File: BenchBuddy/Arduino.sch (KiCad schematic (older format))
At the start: 0 parts

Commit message: Week3 Part 2
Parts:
- added ARD?: ARDUINOPINS, symbol ARDUINOPINS
- added R? (x14): R, ~, symbol R
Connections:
- net labels added: +12P, ADC_CS_N, CURR_MEAS, DAC_CS_N, FAN_MODE, FAN_PWM, GND, LED_EN_PWM, RELAY+, RELAY-, V+_ADJ_MON, V-_ADJ_MON
- net labels removed: CS_N, FAN_EN, LED_EN, LED_FREQ, Relay+, Relay-
- wire segments 0 -> 31

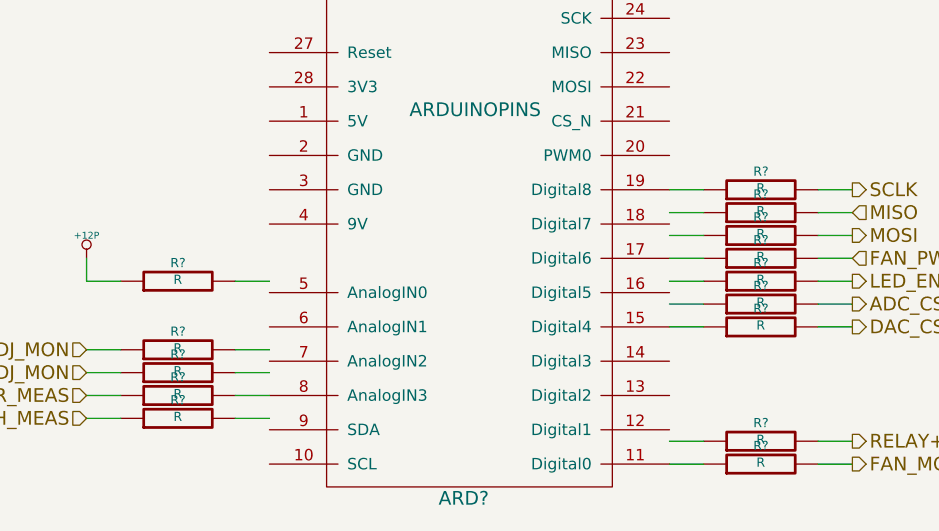
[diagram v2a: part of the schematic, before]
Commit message: Colocação dos Componentes Relé
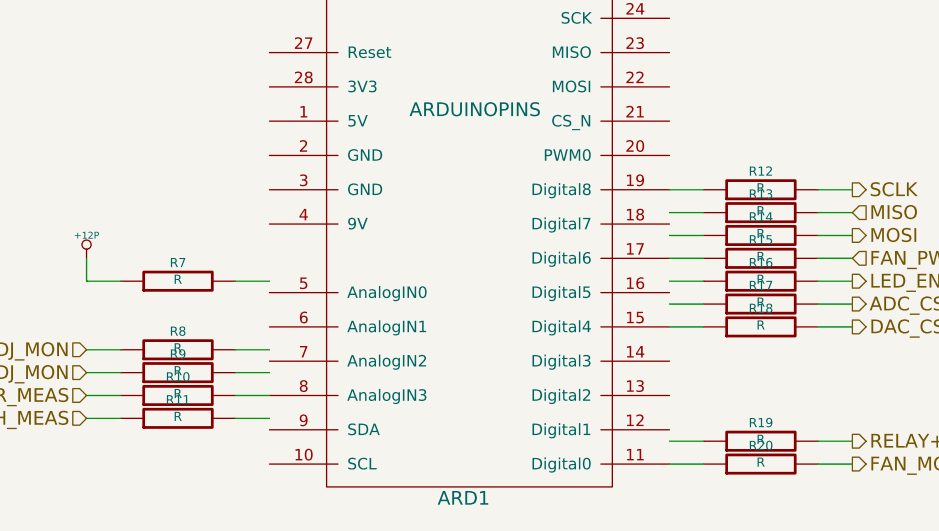
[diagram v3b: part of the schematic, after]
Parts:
- gave numbers to parts that had none: 15
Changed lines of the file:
@@
 Sheet 2 9
 Title ""
-Date "7 mar 2014"
+Date "9 mar 2014"
 Rev ""
 Comp ""
@@
 TACH_MEAS
 $Comp
-L ARDUINOPINS ARD?
+L ARDUINOPINS ARD1
 U 1 1 5319A07F
 P 6200 2900
-F 0 "ARD?" H 6200 2500 60  0000 C CNN
+F 0 "ARD1" H 6200 2500 60  0000 C CNN
 F 1 "ARDUINOPINS" H 6250 4200 60  0000 C CNN
 F 2 "" H 6100 2600 60  0000 C CNN
@@
 CURR_MEAS
 $Comp
-L R R?
+L R R15
 U 1 1 5319A0B5
 P 7500 2250
-F 0 "R?" V 7580 2250 40  0000 C CNN
+F 0 "R15" V 7580 2250 40  0000 C CNN
 F 1 "R" V 7507 2251 40  0000 C CNN
 F 2 "~" V 7430 2250 30  0000 C CNN
@@
 	7750 2250 7900 2250
 $Comp
-L R R?
+L R R19
 U 1 1 5319AB88
 P 7500 3050
-F 0 "R?" V 7580 3050 40  0000 C CNN
+F 0 "R19" V 7580 3050 40  0000 C CNN
 F 1 "R" V 7507 3051 40  0000 C CNN
 F 2 "~" V 7430 3050 30  0000 C CNN
@@
 	9600 2750 9600 3050
 $Comp
-L GND #PWR?
+L GND #PWR2
 U 1 1 5319ABAC
 P 9600 3050
-F 0 "#PWR?" H 9600 3050 30  0001 C CNN
+F 0 "#PWR2" H 9600 3050 30  0001 C CNN
 F 1 "GND" H 9600 2980 30  0001 C CNN
 F 2 "~" H 9600 3050 60  0000 C CNN
@@
 $EndComp
 $Comp
-L R R?
+L R R10
 U 1 1 5319ABC4
 P 4950 2850
-F 0 "R?" V 5030 2850 40  0000 C CNN
+F 0 "R10" V 5030 2850 40  0000 C CNN
 F 1 "R" V 4957 2851 40  0000 C CNN
 F 2 "~" V 4880 2850 30  0000 C CNN
@@
 $EndComp
 $Comp
-L R R?
+L R R11
 U 1 1 5319ABCA
 P 4950 2950
-F 0 "R?" V 5030 2950 40  0000 C CNN
+F 0 "R11" V 5030 2950 40  0000 C CNN
 F 1 "R" V 4957 2951 40  0000 C CNN
 F 2 "~" V 4880 2950 30  0000 C CNN
@@
 V-_ADJ_MON
 $Comp
-L R R?
+L R R9
 U 1 1 5319B50A
 P 4950 2750
-F 0 "R?" V 5030 2750 40  0000 C CNN
+F 0 "R9" V 5030 2750 40  0000 C CNN
 F 1 "R" V 4957 2751 40  0000 C CNN
 F 2 "~" V 4880 2750 30  0000 C CNN
@@
 $EndComp
 $Comp
-L R R?
+L R R8
 U 1 1 5319B510
 P 4950 2650
-F 0 "R?" V 5030 2650 40  0000 C CNN
+F 0 "R8" V 5030 2650 40  0000 C CNN
 F 1 "R" V 4957 2651 40  0000 C CNN
 F 2 "~" V 4880 2650 30  0000 C CNN
@@
 	5350 2650 5200 2650
 $Comp
-L R R?
+L R R12
 U 1 1 5319B558
 P 7500 1950
-F 0 "R?" V 7580 1950 40  0000 C CNN
+F 0 "R12" V 7580 1950 40  0000 C CNN
 F 1 "R" V 7507 1951 40  0000 C CNN
 F 2 "~" V 7430 1950 30  0000 C CNN
@@
 $EndComp
 $Comp
-L R R?
+L R R13
 U 1 1 5319B55E
 P 7500 2050
-F 0 "R?" V 7580 2050 40  0000 C CNN
+F 0 "R13" V 7580 2050 40  0000 C CNN
 F 1 "R" V 7507 2051 40  0000 C CNN
 F 2 "~" V 7430 2050 30  0000 C CNN
@@
 $EndComp
 $Comp
-L R R?
+L R R14
 U 1 1 5319B564
 P 7500 2150
-F 0 "R?" V 7580 2150 40  0000 C CNN
+F 0 "R14" V 7580 2150 40  0000 C CNN
 F 1 "R" V 7507 2151 40  0000 C CNN
 F 2 "~" V 7430 2150 30  0000 C CNN
@@
 $EndComp
 $Comp
-L R R?
+L R R18
 U 1 1 5319B56A
 P 7500 2550
-F 0 "R?" V 7580 2550 40  0000 C CNN
+F 0 "R18" V 7580 2550 40  0000 C CNN
 F 1 "R" V 7507 2551 40  0000 C CNN
 F 2 "~" V 7430 2550 30  0000 C CNN
@@
 LED_EN_PWM
 $Comp
-L R R?
+L R R16
 U 1 1 5319B604
 P 7500 2350
-F 0 "R?" V 7580 2350 40  0000 C CNN
+F 0 "R16" V 7580 2350 40  0000 C CNN
 F 1 "R" V 7507 2351 40  0000 C CNN
 F 2 "~" V 7430 2350 30  0000 C CNN
@@
 ADC_CS_N
 $Comp
-L R R?
+L R R17
 U 1 1 5319D914
 P 7500 2450
-F 0 "R?" V 7580 2450 40  0000 C CNN
+F 0 "R17" V 7580 2450 40  0000 C CNN
 F 1 "R" V 7507 2451 40  0000 C CNN
 F 2 "~" V 7430 2450 30  0000 C CNN
@@
 FAN_MODE
 $Comp
-L R R?
+L R R20
 U 1 1 53193D39
 P 7500 3150
-F 0 "R?" V 7580 3150 40  0000 C CNN
+F 0 "R20" V 7580 3150 40  0000 C CNN
 F 1 "R" V 7507 3151 40  0000 C CNN
 F 2 "~" V 7430 3150 30  0000 C CNN
@@
 	7250 3150 7100 3150
 $Comp
-L R R?
+L R R7
 U 1 1 53193D76
 P 4950 2350
-F 0 "R?" V 5030 2350 40  0000 C CNN
+F 0 "R7" V 5030 2350 40  0000 C CNN
 F 1 "R" V 4957 2351 40  0000 C CNN
 F 2 "~" V 4880 2350 30  0000 C CNN
@@
 	4550 2350 4550 2250
 $Comp
-L +12P #PWR?
+L +12P #PWR1
 U 1 1 53193DBB
 P 4550 2250
-F 0 "#PWR?" H 4550 2220 30  0001 C CNN
+F 0 "#PWR1" H 4550 2220 30  0001 C CNN
 F 1 "+12P" H 4550 2350 30  0000 C CNN
 F 2 "~" H 4550 2250 60  0000 C CNN

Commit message: Pre layout
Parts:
- added R26, R45, R46, R47, R48, R49, R52, R53: R, ~, symbol R
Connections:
- net labels added: +5V, ~ADC_CS, ~DAC_CS, ~DR, ~LADC, ~RESET, ~SHDN
- net labels removed: ADC_CS_N, DAC_CS_N
- wire segments 31 -> 49
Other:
- moved on the sheet: ARD1, R10, R11, R12, R13, R14, R15, R16, R17, R18, R19, R20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

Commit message: Pre layout 2
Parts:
- R10, R11, R12, R13, R14, R15, R16, R17, R18, R19, R20, R26, R45, R46, R47, R48, R49, R52, R53, R7, R8, R9: value R -> 0
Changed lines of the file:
@@
 Sheet 9 9
 Title ""
-Date "30 mar 2014"
+Date "23 apr 2014"
 Rev ""
 Comp ""
@@
 P 7000 3700
 F 0 "R15" V 7080 3700 40  0000 C CNN
-F 1 "R" V 7007 3701 40  0000 C CNN
+F 1 "0" V 7007 3701 40  0000 C CNN
 F 2 "~" V 6930 3700 30  0000 C CNN
 F 3 "~" H 7000 3700 30  0000 C CNN
@@
 P 7000 4300
 F 0 "R19" V 7080 4300 40  0000 C CNN
-F 1 "R" V 7007 4301 40  0000 C CNN
+F 1 "0" V 7007 4301 40  0000 C CNN
 F 2 "~" V 6930 4300 30  0000 C CNN
 F 3 "~" H 7000 4300 30  0000 C CNN
@@
 	9500 4800 9500 5100
 $Comp
-L GND #PWR057
+L GND #PWR059
 U 1 1 5319ABAC
 P 9500 5100
-F 0 "#PWR057" H 9500 5100 30  0001 C CNN
+F 0 "#PWR059" H 9500 5100 30  0001 C CNN
 F 1 "GND" H 9500 5030 30  0001 C CNN
 F 2 "~" H 9500 5100 60  0000 C CNN
@@
 P 4450 4750
 F 0 "R10" V 4530 4750 40  0000 C CNN
-F 1 "R" V 4457 4751 40  0000 C CNN
+F 1 "0" V 4457 4751 40  0000 C CNN
 F 2 "~" V 4380 4750 30  0000 C CNN
 F 3 "~" H 4450 4750 30  0000 C CNN
@@
 P 4450 4900
 F 0 "R11" V 4530 4900 40  0000 C CNN
-F 1 "R" V 4457 4901 40  0000 C CNN
+F 1 "0" V 4457 4901 40  0000 C CNN
 F 2 "~" V 4380 4900 30  0000 C CNN
 F 3 "~" H 4450 4900 30  0000 C CNN
@@
 P 4450 4600
 F 0 "R9" V 4530 4600 40  0000 C CNN
-F 1 "R" V 4457 4601 40  0000 C CNN
+F 1 "0" V 4457 4601 40  0000 C CNN
 F 2 "~" V 4380 4600 30  0000 C CNN
 F 3 "~" H 4450 4600 30  0000 C CNN
@@
 P 4450 4450
 F 0 "R8" V 4530 4450 40  0000 C CNN
-F 1 "R" V 4457 4451 40  0000 C CNN
+F 1 "0" V 4457 4451 40  0000 C CNN
 F 2 "~" V 4380 4450 30  0000 C CNN
 F 3 "~" H 4450 4450 30  0000 C CNN
@@
 P 7000 3250
 F 0 "R12" V 7080 3250 40  0000 C CNN
-F 1 "R" V 7007 3251 40  0000 C CNN
+F 1 "0" V 7007 3251 40  0000 C CNN
 F 2 "~" V 6930 3250 30  0000 C CNN
 F 3 "~" H 7000 3250 30  0000 C CNN
@@
 P 7000 3400
 F 0 "R13" V 7080 3400 40  0000 C CNN
-F 1 "R" V 7007 3401 40  0000 C CNN
+F 1 "0" V 7007 3401 40  0000 C CNN
 F 2 "~" V 6930 3400 30  0000 C CNN
 F 3 "~" H 7000 3400 30  0000 C CNN
@@
 P 7000 3550
 F 0 "R14" V 7080 3550 40  0000 C CNN
-F 1 "R" V 7007 3551 40  0000 C CNN
+F 1 "0" V 7007 3551 40  0000 C CNN
 F 2 "~" V 6930 3550 30  0000 C CNN
 F 3 "~" H 7000 3550 30  0000 C CNN
@@
 P 7000 4150
 F 0 "R18" V 7080 4150 40  0000 C CNN
-F 1 "R" V 7007 4151 40  0000 C CNN
+F 1 "0" V 7007 4151 40  0000 C CNN
 F 2 "~" V 6930 4150 30  0000 C CNN
 F 3 "~" H 7000 4150 30  0000 C CNN
@@
 P 7000 3850
 F 0 "R16" V 7080 3850 40  0000 C CNN
-F 1 "R" V 7007 3851 40  0000 C CNN
+F 1 "0" V 7007 3851 40  0000 C CNN
 F 2 "~" V 6930 3850 30  0000 C CNN
 F 3 "~" H 7000 3850 30  0000 C CNN
@@
 P 7000 4000
 F 0 "R17" V 7080 4000 40  0000 C CNN
-F 1 "R" V 7007 4001 40  0000 C CNN
+F 1 "0" V 7007 4001 40  0000 C CNN
 F 2 "~" V 6930 4000 30  0000 C CNN
 F 3 "~" H 7000 4000 30  0000 C CNN
@@
 P 7000 5200
 F 0 "R20" V 7080 5200 40  0000 C CNN
-F 1 "R" V 7007 5201 40  0000 C CNN
+F 1 "0" V 7007 5201 40  0000 C CNN
 F 2 "~" V 6930 5200 30  0000 C CNN
 F 3 "~" H 7000 5200 30  0000 C CNN
@@
 P 4450 4150
 F 0 "R7" V 4530 4150 40  0000 C CNN
-F 1 "R" V 4457 4151 40  0000 C CNN
+F 1 "0" V 4457 4151 40  0000 C CNN
 F 2 "~" V 4380 4150 30  0000 C CNN
 F 3 "~" H 4450 4150 30  0000 C CNN
@@
 	3500 4150 3500 4050
 $Comp
-L +12P #PWR058
+L +12P #PWR060
 U 1 1 53193DBB
 P 3500 4050
-F 0 "#PWR058" H 3500 4020 30  0001 C CNN
+F 0 "#PWR060" H 3500 4020 30  0001 C CNN
 F 1 "+12P" H 3500 4150 30  0000 C CNN
 F 2 "~" H 3500 4050 60  0000 C CNN
@@
 P 7000 4450
 F 0 "R45" V 7080 4450 40  0000 C CNN
-F 1 "R" V 7007 4451 40  0000 C CNN
+F 1 "0" V 7007 4451 40  0000 C CNN
 F 2 "~" V 6930 4450 30  0000 C CNN
 F 3 "~" H 7000 4450 30  0000 C CNN
@@
 P 7000 4600
 F 0 "R46" V 7080 4600 40  0000 C CNN
-F 1 "R" V 7007 4601 40  0000 C CNN
+F 1 "0" V 7007 4601 40  0000 C CNN
 F 2 "~" V 6930 4600 30  0000 C CNN
 F 3 "~" H 7000 4600 30  0000 C CNN
@@
 P 4450 4000
 F 0 "R49" V 4530 4000 40  0000 C CNN
-F 1 "R" V 4457 4001 40  0000 C CNN
+F 1 "0" V 4457 4001 40  0000 C CNN
 F 2 "~" V 4380 4000 30  0000 C CNN
 F 3 "~" H 4450 4000 30  0000 C CNN
@@
 P 4450 3850
 F 0 "R48" V 4530 3850 40  0000 C CNN
-F 1 "R" V 4457 3851 40  0000 C CNN
+F 1 "0" V 4457 3851 40  0000 C CNN
 F 2 "~" V 4380 3850 30  0000 C CNN
 F 3 "~" H 4450 3850 30  0000 C CNN
@@
 P 4450 3700
 F 0 "R47" V 4530 3700 40  0000 C CNN
-F 1 "R" V 4457 3701 40  0000 C CNN
+F 1 "0" V 4457 3701 40  0000 C CNN
 F 2 "~" V 4380 3700 30  0000 C CNN
 F 3 "~" H 4450 3700 30  0000 C CNN
@@
 Connection ~ 3950 3850
 $Comp
-L GND #PWR059
+L GND #PWR061
 U 1 1 53246B1E
 P 3750 3950
-F 0 "#PWR059" H 3750 3950 30  0001 C CNN
+F 0 "#PWR061" H 3750 3950 30  0001 C CNN
 F 1 "GND" H 3750 3880 30  0001 C CNN
 F 2 "~" H 3750 3950 60  0000 C CNN
@@
 $EndComp
 $Comp
-L +5V #PWR060
+L +5V #PWR062
 U 1 1 53246B4F
 P 3500 3550
-F 0 "#PWR060" H 3500 3640 20  0001 C CNN
+F 0 "#PWR062" H 3500 3640 20  0001 C CNN
 F 1 "+5V" H 3500 3640 30  0000 C CNN
 F 2 "~" H 3500 3550 60  0000 C CNN
@@
 P 9000 4800
 F 0 "R26" V 9080 4800 40  0000 C CNN
-F 1 "R" V 9007 4801 40  0000 C CNN
+F 1 "0" V 9007 4801 40  0000 C CNN
 F 2 "~" V 8930 4800 30  0000 C CNN
 F 3 "~" H 9000 4800 30  0000 C CNN
@@
 P 7000 4750
 F 0 "R52" V 7080 4750 40  0000 C CNN
-F 1 "R" V 7007 4751 40  0000 C CNN
+F 1 "0" V 7007 4751 40  0000 C CNN
 F 2 "~" V 6930 4750 30  0000 C CNN
 F 3 "~" H 7000 4750 30  0000 C CNN
@@
 P 7000 4900
 F 0 "R53" V 7080 4900 40  0000 C CNN
-F 1 "R" V 7007 4901 40  0000 C CNN
+F 1 "0" V 7007 4901 40  0000 C CNN
 F 2 "~" V 6930 4900 30  0000 C CNN
 F 3 "~" H 7000 4900 30  0000 C CNN
